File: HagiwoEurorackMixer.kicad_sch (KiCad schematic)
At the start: 22 parts, among them J1 IN1, J2 IN2, J3 IN3, J4 IN4, J5 OUT, J7 Eurorack_Power_10pin_Unshroud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, U2 TL072

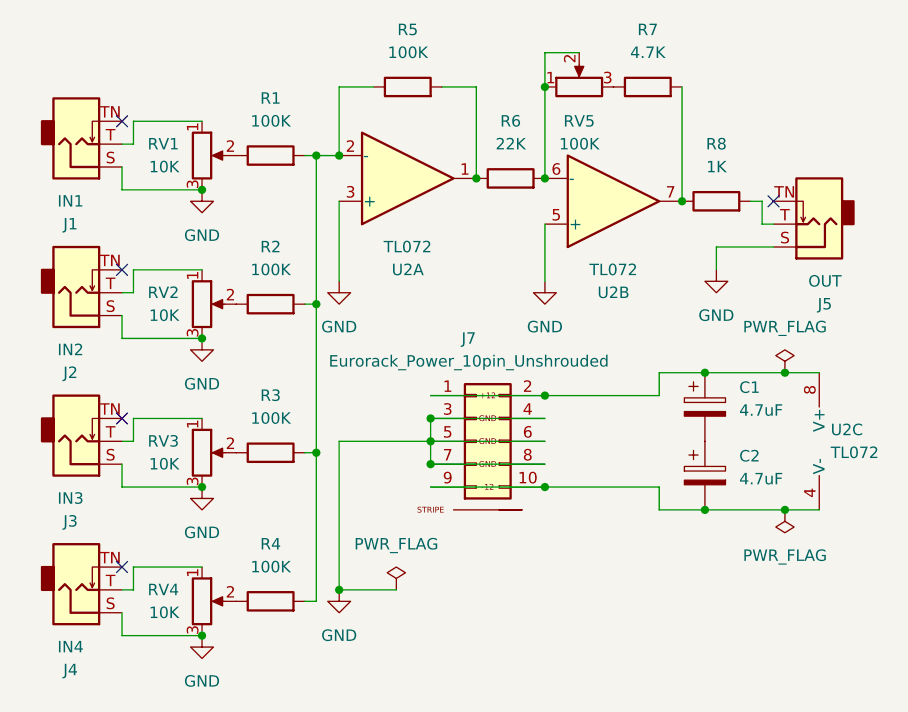
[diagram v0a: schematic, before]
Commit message: laid out V1.1 again for better placement
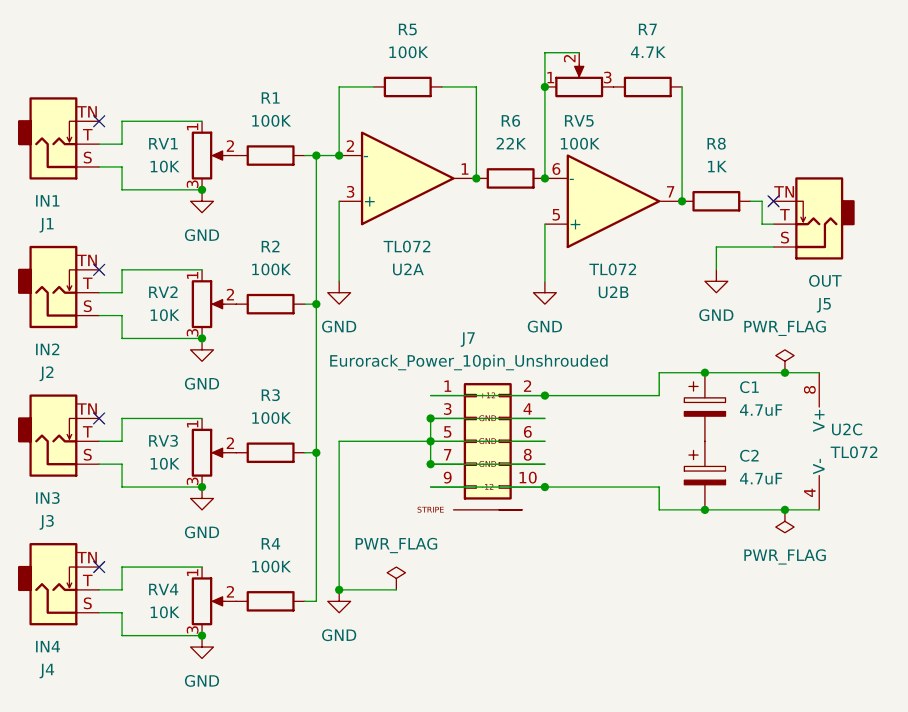
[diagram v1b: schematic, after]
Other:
- moved on the sheet: J1, J2, J3, J4
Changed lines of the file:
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@@
 	)
 	(no_connect
-		(at 40.64 34.29)
+		(at 38.1 34.29)
 	)
 	(no_connect
-		(at 40.64 83.82)
+		(at 38.1 83.82)
 	)
 	(no_connect
-		(at 40.64 67.31)
+		(at 38.1 67.31)
 	)
 	(no_connect
@@
 	)
 	(no_connect
-		(at 40.64 50.8)
-	)
-	(wire
-		(pts
-			(xy 41.91 86.36) (xy 41.91 83.82)
-		)
-		(stroke
-			(width 0)
-			(type default)
-		)
+		(at 38.1 50.8)
 	)
 	(wire
@@
 	(wire
 		(pts
-			(xy 40.64 69.85) (xy 41.91 69.85)
+			(xy 38.1 88.9) (xy 40.64 88.9)
 		)
 		(stroke
@@
 	(wire
 		(pts
+			(xy 38.1 39.37) (xy 40.64 39.37)
+		)
+		(stroke
+			(width 0)
+			(type default)
+		)
+	)
+	(wire
+		(pts
 			(xy 64.77 69.85) (xy 74.93 69.85)
 		)
@@
 	(wire
 		(pts
-			(xy 41.91 53.34) (xy 41.91 50.8)
+			(xy 40.64 53.34) (xy 40.64 50.8)
 		)
 		(stroke
@@
 	(wire
 		(pts
-			(xy 41.91 69.85) (xy 41.91 67.31)
+			(xy 38.1 55.88) (xy 40.64 55.88)
+		)
+		(stroke
+			(width 0)
+			(type default)
+		)
+	)
+	(wire
+		(pts
+			(xy 40.64 69.85) (xy 40.64 67.31)
 		)
 		(stroke
@@
 	(wire
 		(pts
-			(xy 40.64 36.83) (xy 41.91 36.83)
-		)
-		(stroke
-			(width 0)
-			(type default)
-		)
-	)
-	(wire
-		(pts
 			(xy 62.23 38.1) (xy 64.77 38.1)
 		)
@@
 	(wire
 		(pts
-			(xy 41.91 36.83) (xy 41.91 34.29)
+			(xy 40.64 36.83) (xy 40.64 34.29)
 		)
 		(stroke
@@
 	(wire
 		(pts
-			(xy 41.91 50.8) (xy 49.53 50.8)
+			(xy 40.64 50.8) (xy 49.53 50.8)
 		)
 		(stroke
@@
 	(wire
 		(pts
-			(xy 40.64 86.36) (xy 41.91 86.36)
-		)
-		(stroke
-			(width 0)
-			(type default)
-		)
-	)
-	(wire
-		(pts
 			(xy 60.96 54.61) (xy 62.23 54.61)
 		)
@@
 	(wire
 		(pts
-			(xy 41.91 34.29) (xy 49.53 34.29)
+			(xy 40.64 34.29) (xy 49.53 34.29)
+		)
+		(stroke
+			(width 0)
+			(type default)
+		)
+	)
+	(wire
+		(pts
+			(xy 38.1 36.83) (xy 40.64 36.83)
 		)
 		(stroke
@@
 	(wire
 		(pts
-			(xy 41.91 83.82) (xy 49.53 83.82)
+			(xy 38.1 72.39) (xy 40.64 72.39)
+		)
+		(stroke
+			(width 0)
+			(type default)
+		)
+	)
+	(wire
+		(pts
+			(xy 40.64 83.82) (xy 49.53 83.82)
+		)
+		(stroke
+			(width 0)
+			(type default)
+		)
+	)
+	(wire
+		(pts
+			(xy 38.1 53.34) (xy 40.64 53.34)
 		)
 		(stroke
@@
 	(wire
 		(pts
-			(xy 41.91 67.31) (xy 49.53 67.31)
+			(xy 40.64 83.82) (xy 40.64 86.36)
+		)
+		(stroke
+			(width 0)
+			(type default)
+		)
+	)
+	(wire
+		(pts
+			(xy 40.64 67.31) (xy 49.53 67.31)
 		)
 		(stroke
@@
 	(wire
 		(pts
+			(xy 38.1 69.85) (xy 40.64 69.85)
+		)
+		(stroke
+			(width 0)
+			(type default)
+		)
+	)
+	(wire
+		(pts
 			(xy 40.64 58.42) (xy 40.64 55.88)
 		)
@@
 	(wire
 		(pts
-			(xy 40.64 53.34) (xy 41.91 53.34)
+			(xy 38.1 86.36) (xy 40.64 86.36)
 		)
 		(stroke
@@
 	(symbol
 		(lib_id "Connector_Audio:AudioJack2_SwitchT")
-		(at 35.56 86.36 0)
+		(at 33.02 86.36 0)
 		(mirror x)
 		(unit 1)
@@
 		(dnp no)
 		(property "Reference" "J4"
-			(at 34.925 95.25 0)
+			(at 32.385 95.25 0)
 			(effects
 				(font
@@
 		)
 		(property "Value" "IN4"
-			(at 34.925 92.71 0)
+			(at 32.385 92.71 0)
 			(effects
 				(font
@@
 		)
 		(property "Footprint" "Library:EighthInch_PJ398SM_T_TN_S"
-			(at 35.56 86.36 0)
+			(at 33.02 86.36 0)
 			(effects
 				(font
@@
 		)
 		(property "Datasheet" "~"
-			(at 35.56 86.36 0)
+			(at 33.02 86.36 0)
 			(effects
 				(font
@@
 		)
 		(property "Description" ""
-			(at 35.56 86.36 0)
+			(at 33.02 86.36 0)
 			(effects
 				(font
@@
 		(fields_autoplaced yes)
 		(property "Reference" "RV1"
-			(at 46.99 36.83 0)
+			(at 46.99 36.8299 0)
 			(effects
 				(font
@@
 		)
 		(property "Value" "10K"
-			(at 46.99 39.37 0)
+			(at 46.99 39.3699 0)
 			(effects
 				(font
@@
 	(symbol
 		(lib_id "Connector_Audio:AudioJack2_SwitchT")
-		(at 35.56 69.85 0)
+		(at 33.02 69.85 0)
 		(mirror x)
 		(unit 1)
@@
 		(dnp no)
 		(property "Reference" "J3"
-			(at 34.925 78.74 0)
+			(at 32.385 78.74 0)
 			(effects
 				(font
@@
 		)
 		(property "Value" "IN3"
-			(at 34.925 76.2 0)
+			(at 32.385 76.2 0)
 			(effects
 				(font
@@
 		)
 		(property "Footprint" "Library:EighthInch_PJ398SM_T_TN_S"
-			(at 35.56 69.85 0)
+			(at 33.02 69.85 0)
 			(effects
 				(font
@@
 		)
 		(property "Datasheet" "~"
-			(at 35.56 69.85 0)
+			(at 33.02 69.85 0)
 			(effects
 				(font
@@
 		)
 		(property "Description" ""
-			(at 35.56 69.85 0)
+			(at 33.02 69.85 0)
 			(effects
 				(font
@@
 	(symbol
 		(lib_id "Connector_Audio:AudioJack2_SwitchT")
-		(at 35.56 36.83 0)
+		(at 33.02 36.83 0)
 		(mirror x)
 		(unit 1)
@@
 		(dnp no)
 		(property "Reference" "J1"
-			(at 34.925 45.72 0)
+			(at 32.385 45.72 0)
 			(effects
 				(font
@@
 		)
 		(property "Value" "IN1"
-			(at 34.925 43.18 0)
+			(at 32.385 43.18 0)
 			(effects
 				(font
@@
 		)
 		(property "Footprint" "Library:EighthInch_PJ398SM_T_TN_S"
-			(at 35.56 36.83 0)
+			(at 33.02 36.83 0)
 			(effects
 				(font
@@
 		)
 		(property "Datasheet" "~"
-			(at 35.56 36.83 0)
+			(at 33.02 36.83 0)
 			(effects
 				(font
@@
 		)
 		(property "Description" ""
-			(at 35.56 36.83 0)
+			(at 33.02 36.83 0)
 			(effects
 				(font
@@
 		(fields_autoplaced yes)
 		(property "Reference" "RV4"
-			(at 46.99 86.36 0)
+			(at 46.99 86.3599 0)
 			(effects
 				(font
@@
 		)
 		(property "Value" "10K"
-			(at 46.99 88.9 0)
+			(at 46.99 88.8999 0)
 			(effects
 				(font
@@
 	(symbol
 		(lib_id "Connector_Audio:AudioJack2_SwitchT")
-		(at 35.56 53.34 0)
+		(at 33.02 53.34 0)
 		(mirror x)
 		(unit 1)
@@
 		(dnp no)
 		(property "Reference" "J2"
-			(at 34.925 62.23 0)
+			(at 32.385 62.23 0)
 			(effects
 				(font
@@
 		)
 		(property "Value" "IN2"
-			(at 34.925 59.69 0)
+			(at 32.385 59.69 0)
 			(effects
 				(font
@@
 		)
 		(property "Footprint" "Library:EighthInch_PJ398SM_T_TN_S"
-			(at 35.56 53.34 0)
+			(at 33.02 53.34 0)
 			(effects
 				(font
@@
 		)
 		(property "Datasheet" "~"
-			(at 35.56 53.34 0)
+			(at 33.02 53.34 0)
 			(effects
 				(font
@@
 		)
 		(property "Description" ""
-			(at 35.56 53.34 0)
+			(at 33.02 53.34 0)
 			(effects
 				(font
@@
 		(on_board yes)
 		(dnp no)
-		(fields_autoplaced yes)
 		(property "Reference" "RV5"
 			(at 91.44 34.29 90)
@@
 		(fields_autoplaced yes)
 		(property "Reference" "RV2"
-			(at 46.99 53.34 0)
+			(at 46.99 53.3399 0)
 			(effects
 				(font
@@
 		)
 		(property "Value" "10K"
-			(at 46.99 55.88 0)
+			(at 46.99 55.8799 0)
 			(effects
 				(font
@@
 		(fields_autoplaced yes)
 		(property "Reference" "RV3"
-			(at 46.99 69.85 0)
+			(at 46.99 69.8499 0)
 			(effects
 				(font
@@
 		)
 		(property "Value" "10K"
-			(at 46.99 72.39 0)
-			(effects
-				(font
+			(at 46.99 72.3899 0)
+			(effects
+				(font

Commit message: laid out V1.1 again for better placement
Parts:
- RV5: footprint LibraryAll:Pot_9mm_DShaft_RemovedPins4_5 -> Library:Pot_9mm_DShaft_RemovedPins4_5
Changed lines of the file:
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@@
 			)
 		)
-		(property "Footprint" "LibraryAll:Pot_9mm_DShaft_RemovedPins4_5"
+		(property "Footprint" "Library:Pot_9mm_DShaft_RemovedPins4_5"
 			(at 91.44 30.48 0)
 			(effects

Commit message: v1.2 ready for production - slightly unsure if volume pot left/right side wiring is correct
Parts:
- added D1, D2: 1N5817, Diode_THT:D_DO-41_SOD81_P10.16mm_Horizontal, symbol Device:D
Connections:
- net GND: now also RV1.1, RV2.1, RV3.1, RV4.1; no longer RV1.3, RV2.3, RV3.3, RV4.3
- net at J4.T: now also RV4.3; no longer RV4.1
- net at R7.1: now also RV5.1; no longer RV5.3
- net at J1.T: now also RV1.3; no longer RV1.1
- net at J3.T: now also RV3.3; no longer RV3.1
- net at C2.2, U2.4 (V-): now also D2.2 (A); no longer J7.10 (-12V), J7.9 (-12V)
- net at C1.1, U2.8 (V+): now also D1.1 (K); no longer J7.1 (+12V), J7.2 (+12V)
- net at J2.T: now also RV2.3; no longer RV2.1
- net at R6.2, RV5.2, U2.6 (-): now also RV5.3; no longer RV5.1
- new net: D1.2 (A), J7.1 (+12V), J7.2 (+12V)
- new net: D2.1 (K), J7.10 (-12V), J7.9 (-12V)
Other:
- moved on the sheet: RV5
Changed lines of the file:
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@@
 	)
 	(junction
-		(at 49.53 41.91)
+		(at 87.63 74.93)
 		(diameter 0)
 		(color 0 0 0 0)
@@
 	)
 	(junction
-		(at 64.77 86.36)
+		(at 49.53 41.91)
 		(diameter 0)
 		(color 0 0 0 0)
 	)
 	(junction
-		(at 49.53 58.42)
+		(at 64.77 86.36)
 		(diameter 0)
 		(color 0 0 0 0)
 	)
 	(junction
-		(at 49.53 91.44)
+		(at 49.53 58.42)
 		(diameter 0)
 		(color 0 0 0 0)
@@
 	)
 	(junction
-		(at 114.3 62.23)
+		(at 49.53 74.93)
 		(diameter 0)
 		(color 0 0 0 0)
 	)
 	(junction
-		(at 87.63 40.64)
+		(at 114.3 62.23)
 		(diameter 0)
 		(color 0 0 0 0)
 	)
 	(junction
-		(at 62.23 38.1)
+		(at 87.63 40.64)
 		(diameter 0)
 		(color 0 0 0 0)
 	)
 	(junction
-		(at 49.53 74.93)
+		(at 62.23 38.1)
 		(diameter 0)
 		(color 0 0 0 0)
 	)
 	(junction
-		(at 105.41 62.23)
+		(at 87.63 64.77)
 		(diameter 0)
 		(color 0 0 0 0)
 	)
 	(junction
-		(at 87.63 74.93)
+		(at 105.41 62.23)
 		(diameter 0)
 		(color 0 0 0 0)
@@
 	)
 	(junction
-		(at 87.63 64.77)
+		(at 87.63 30.48)
 		(diameter 0)
 		(color 0 0 0 0)
 	)
 	(junction
-		(at 87.63 30.48)
+		(at 49.53 91.44)
 		(diameter 0)
 		(color 0 0 0 0)
@@
 	(wire
 		(pts
-			(xy 87.63 64.77) (xy 100.33 64.77)
-		)
-		(stroke
-			(width 0)
-			(type default)
-		)
-	)
-	(wire
-		(pts
 			(xy 74.93 74.93) (xy 87.63 74.93)
 		)
@@
 	(wire
 		(pts
+			(xy 87.63 74.93) (xy 90.17 74.93)
+		)
+		(stroke
+			(width 0)
+			(type default)
+		)
+	)
+	(wire
+		(pts
 			(xy 64.77 43.18) (xy 64.77 52.07)
 		)
@@
 	(wire
 		(pts
+			(xy 97.79 74.93) (xy 100.33 74.93)
+		)
+		(stroke
+			(width 0)
+			(type default)
+		)
+	)
+	(wire
+		(pts
 			(xy 49.53 91.44) (xy 40.64 91.44)
 		)
@@
 	(wire
 		(pts
+			(xy 87.63 64.77) (xy 90.17 64.77)
+		)
+		(stroke
+			(width 0)
+			(type default)
+		)
+	)
+	(wire
+		(pts
 			(xy 60.96 71.12) (xy 62.23 71.12)
 		)
@@
 	(wire
 		(pts
-			(xy 100.33 64.77) (xy 100.33 62.23)
+			(xy 97.79 64.77) (xy 100.33 64.77)
 		)
 		(stroke
@@
 	(wire
 		(pts
-			(xy 40.64 83.82) (xy 40.64 86.36)
+			(xy 100.33 64.77) (xy 100.33 62.23)
 		)
 		(stroke
@@
 	(wire
 		(pts
-			(xy 40.64 67.31) (xy 49.53 67.31)
+			(xy 40.64 83.82) (xy 40.64 86.36)
 		)
 		(stroke
@@
 	(wire
 		(pts
-			(xy 60.96 87.63) (xy 62.23 87.63)
+			(xy 40.64 67.31) (xy 49.53 67.31)
 		)
 		(stroke
@@
 	(wire
 		(pts
-			(xy 100.33 74.93) (xy 100.33 77.47)
+			(xy 60.96 87.63) (xy 62.23 87.63)
 		)
 		(stroke
@@
 	(wire
 		(pts
-			(xy 74.93 69.85) (xy 74.93 72.39)
+			(xy 100.33 74.93) (xy 100.33 77.47)
 		)
 		(stroke
@@
 	(wire
 		(pts
-			(xy 49.53 58.42) (xy 40.64 58.42)
+			(xy 74.93 69.85) (xy 74.93 72.39)
 		)
 		(stroke
@@
 	(wire
 		(pts
-			(xy 87.63 74.93) (xy 100.33 74.93)
+			(xy 49.53 58.42) (xy 40.64 58.42)
 		)
 		(stroke
@@
 		(lib_id "Device:R_Potentiometer")
 		(at 49.53 38.1 0)
+		(mirror x)
 		(unit 1)
 		(exclude_from_sim no)
@@
 		(on_board yes)
 		(dnp no)
-		(fields_autoplaced yes)
 		(property "Reference" "RV1"
 			(at 46.99 36.8299 0)
@@
 		(lib_id "Device:R_Potentiometer")
 		(at 49.53 87.63 0)
+		(mirror x)
 		(unit 1)
 		(exclude_from_sim no)
@@
 		(on_board yes)
 		(dnp no)
-		(fields_autoplaced yes)
 		(property "Reference" "RV4"
 			(at 46.99 86.3599 0)
@@
 	)
 	(symbol
+		(lib_id "Device:D")
+		(at 93.98 64.77 0)
+		(mirror y)
+		(unit 1)
+		(exclude_from_sim no)
+		(in_bom yes)
+		(on_board yes)
+		(dnp no)
+		(property "Reference" "D1"
+			(at 93.98 71.12 0)
+			(effects
+				(font
+					(size 1.27 1.27)
+				)
+			)
+		)
+		(property "Value" "1N5817"
+			(at 93.98 68.58 0)
+			(effects
+				(font
+					(size 1.27 1.27)
+				)
+			)
+		)
+		(property "Footprint" "Diode_THT:D_DO-41_SOD81_P10.16mm_Horizontal"
+			(at 93.98 64.77 0)
+			(effects
+				(font
+					(size 1.27 1.27)
+				)
+				(hide yes)
+			)
+		)
+		(property "Datasheet" "~"
+			(at 93.98 64.77 0)
+			(effects
+				(font
+					(size 1.27 1.27)
+				)
+				(hide yes)
+			)
+		)
+		(property "Description" "Diode"
+			(at 93.98 64.77 0)
+			(effects
+				(font
+					(size 1.27 1.27)
+				)
+				(hide yes)
+			)
+		)
+		(property "Sim.Device" "D"
+			(at 93.98 64.77 0)
+			(effects
+				(font
+					(size 1.27 1.27)
+				)
+				(hide yes)
+			)
+		)
+		(property "Sim.Pins" "1=K 2=A"
+			(at 93.98 64.77 0)
+			(effects
+				(font
+					(size 1.27 1.27)
+				)
+				(hide yes)
+			)
+		)
+		(pin "2"
+		)
+		(pin "1"
+		)
+		(instances
+			(project "HagiwoEurorackMixer"
+				(path "/56bf8528-2dcc-4e9e-a6bb-ed2d17ee9d21"
+					(reference "D1")
+					(unit 1)
+				)
+			)
+		)
+	)
+	(symbol
+		(lib_id "Device:D")
+		(at 93.98 74.93 0)
+		(mirror x)
+		(unit 1)
+		(exclude_from_sim no)
+		(in_bom yes)
+		(on_board yes)
+		(dnp no)
+		(property "Reference" "D2"
+			(at 93.98 81.28 0)
+			(effects
+				(font
+					(size 1.27 1.27)
+				)
+			)
+		)
+		(property "Value" "1N5817"
+			(at 93.98 78.74 0)
+			(effects
+				(font
+					(size 1.27 1.27)
+				)
+			)
+		)
+		(property "Footprint" "Diode_THT:D_DO-41_SOD81_P10.16mm_Horizontal"
+			(at 93.98 74.93 0)
+			(effects
+				(font
+					(size 1.27 1.27)
+				)
+				(hide yes)
+			)
+		)
+		(property "Datasheet" "~"
+			(at 93.98 74.93 0)
+			(effects
+				(font
+					(size 1.27 1.27)
+				)
+				(hide yes)
+			)
+		)
+		(property "Description" "Diode"
+			(at 93.98 74.93 0)
+			(effects
+				(font
+					(size 1.27 1.27)
+				)
+				(hide yes)
+			)
+		)
+		(property "Sim.Device" "D"
+			(at 93.98 74.93 0)
+			(effects
+				(font
+					(size 1.27 1.27)
+				)
+				(hide yes)
+			)
+		)
+		(property "Sim.Pins" "1=K 2=A"
+			(at 93.98 74.93 0)
+			(effects
+				(font
+					(size 1.27 1.27)
+				)
+				(hide yes)
+			)
+		)
+		(pin "2"
+		)
+		(pin "1"
+		)
+		(instances
+			(project "HagiwoEurorackMixer"
+				(path "/56bf8528-2dcc-4e9e-a6bb-ed2d17ee9d21"
+					(reference "D2")
+					(unit 1)
+				)
+			)
+		)
+	)
+	(symbol
 		(lib_id "Device:R_Potentiometer")
-		(at 91.44 30.48 90)
+		(at 91.44 30.48 270)
+		(mirror x)
 		(unit 1)
 		(exclude_from_sim no)
@@
 		(lib_id "Device:R_Potentiometer")
 		(at 49.53 54.61 0)
+		(mirror x)
 		(unit 1)
 		(exclude_from_sim no)
@@
 		(on_board yes)
 		(dnp no)
-		(fields_autoplaced yes)
 		(property "Reference" "RV2"
 			(at 46.99 53.3399 0)
@@
 		(lib_id "Device:R_Potentiometer")
 		(at 49.53 71.12 0)
+		(mirror x)
 		(unit 1)
 		(exclude_from_sim no)
@@
 		(on_board yes)
 		(dnp no)
-		(fields_autoplaced yes)
 		(property "Reference" "RV3"
 			(at 46.99 69.8499 0)
